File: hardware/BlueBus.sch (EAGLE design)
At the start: 128 parts, among them Q1 NMOSFET-BSS138K, Q2 PMOSFET-DMP1045UQ, Q3 NMOSFET-BSS138K, X1 CRYSTAL-12MHZ

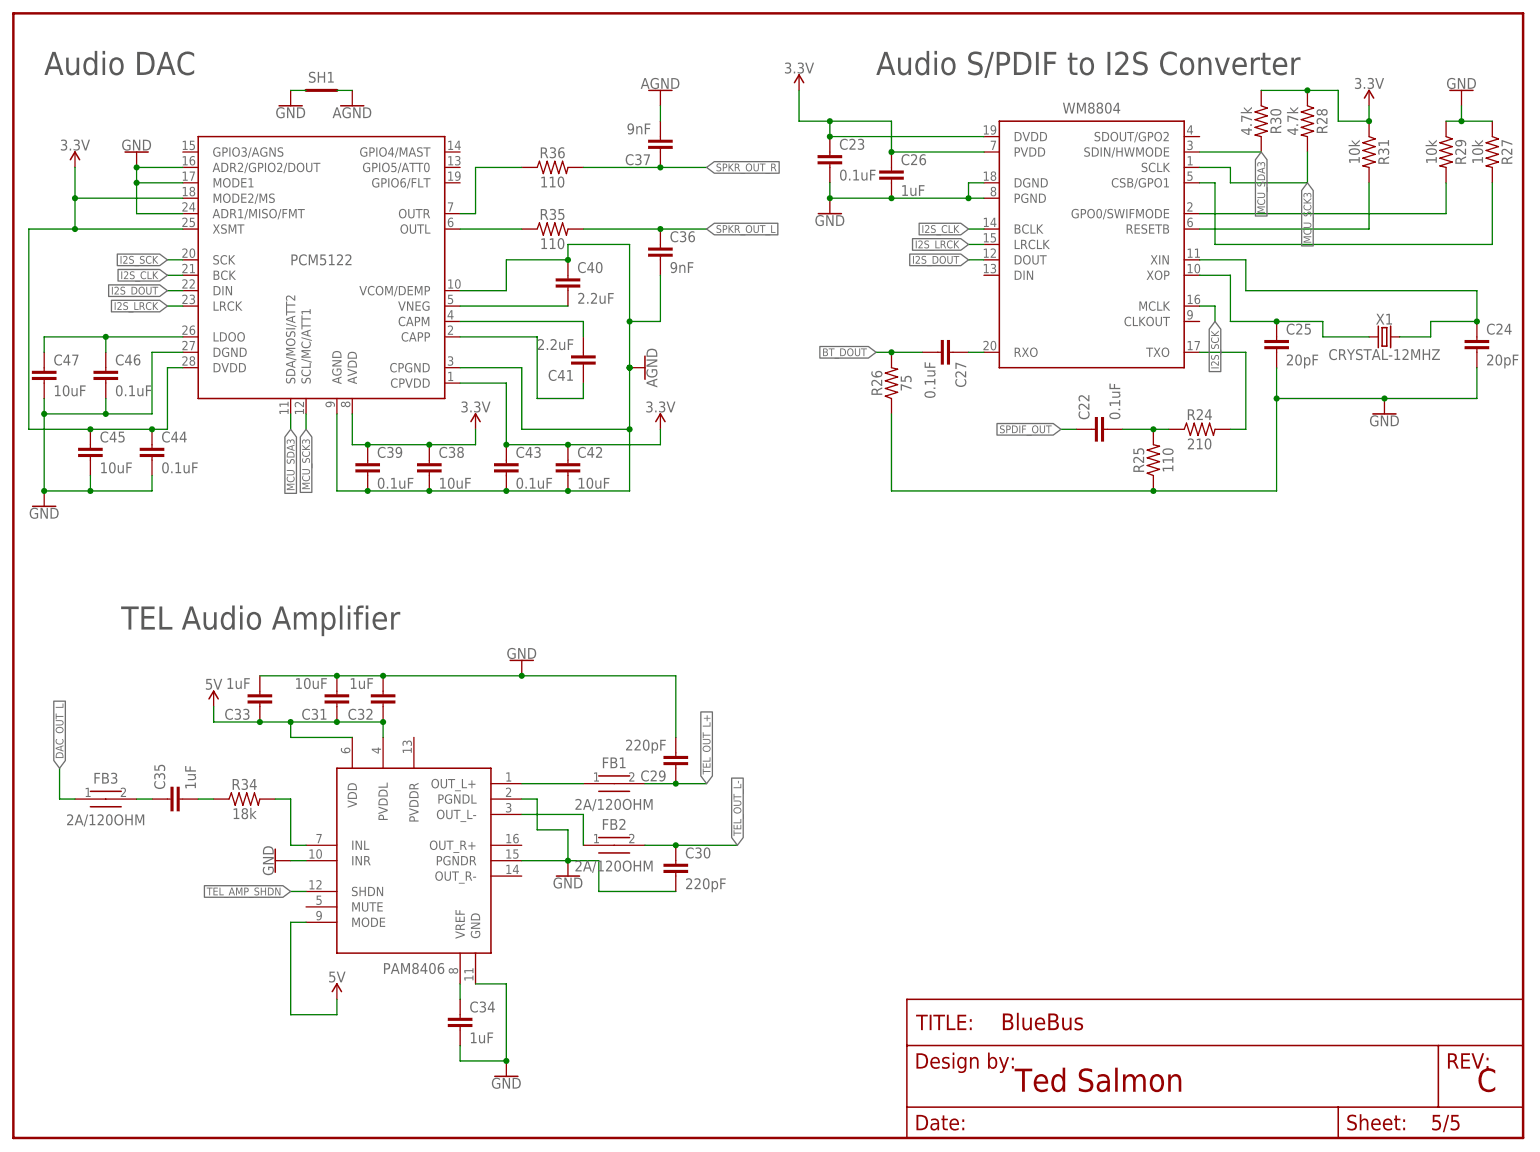
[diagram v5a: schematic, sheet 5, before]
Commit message: [IMP] hardware: V 1.2 * Power PAM8406 PVDDR and add bypass caps * Rework layout for PAM8406 and its passives * Connect floating VIAs to ground
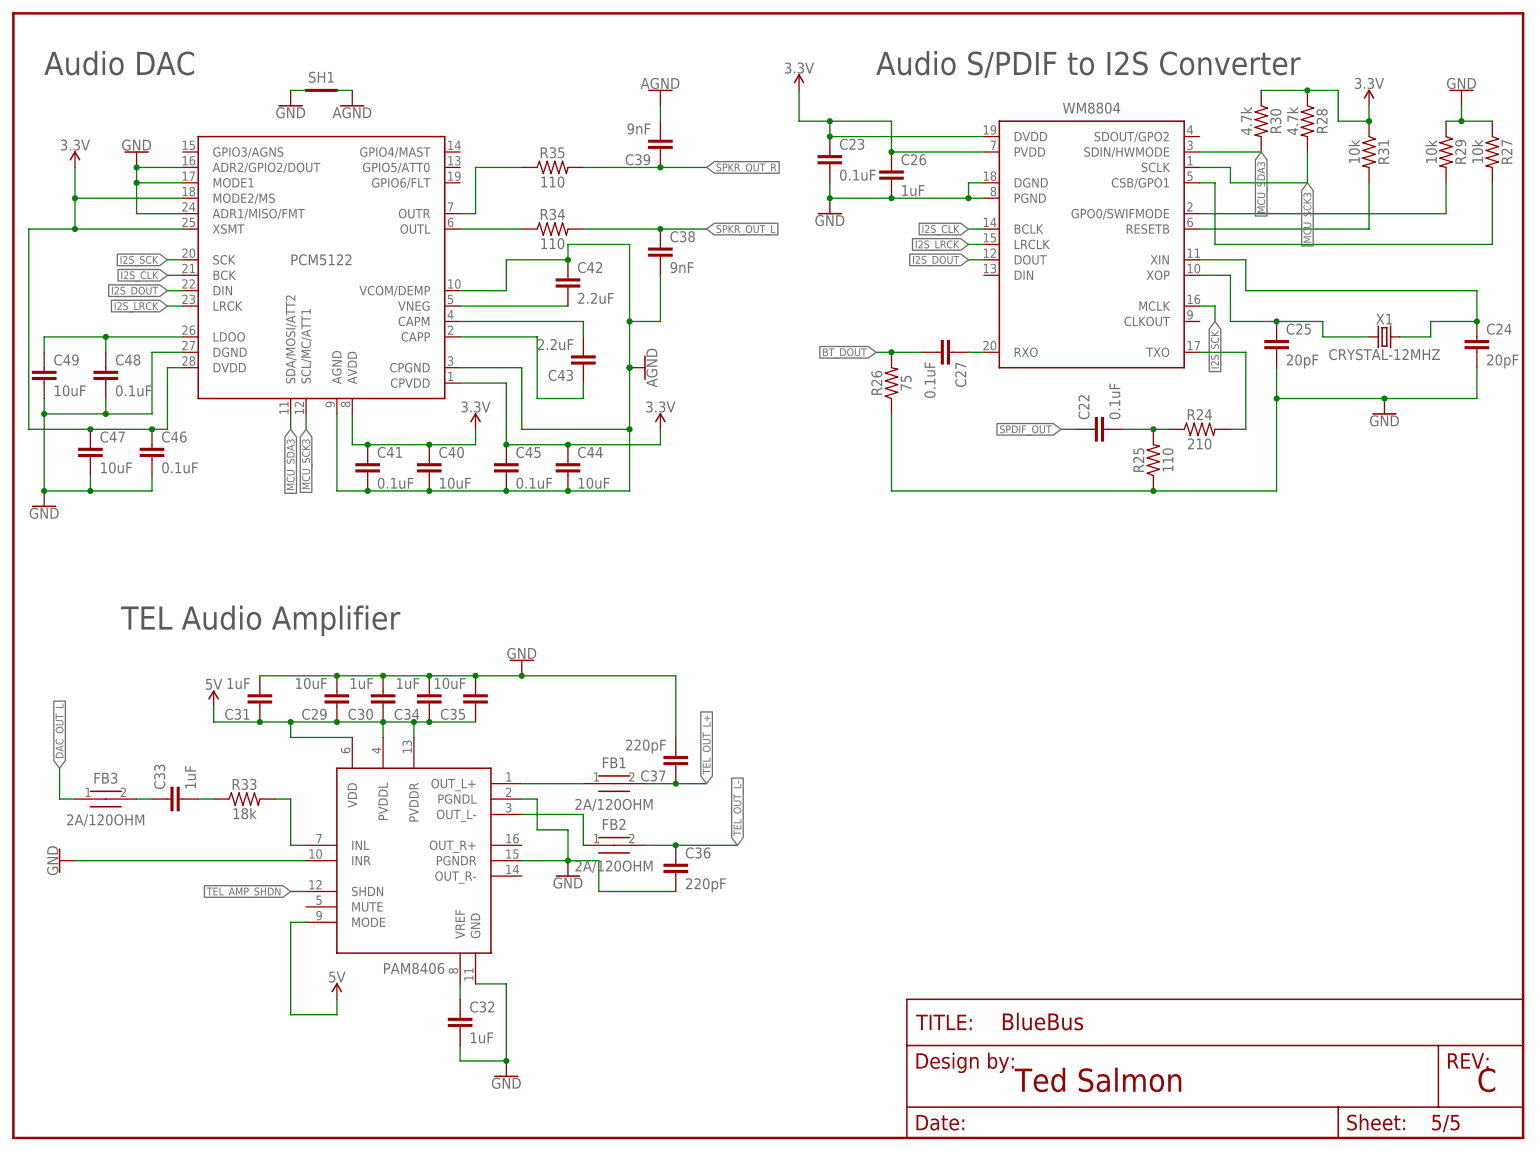
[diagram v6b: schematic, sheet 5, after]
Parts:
- removed R36: 110, Passives:110OHM
- added C48: 0.1uF, Passives:0.1UF
- added C49: 10uF, Passives:10UF2012
- added R33: 18k, Passives:18KOHM
- C29: value 220pF -> 10uF; device Passives:220PF -> Passives:10UF2012
- C30: value 220pF -> 1uF; device Passives:220PF -> Passives:1UF
- C31: value 10uF -> 1uF; device Passives:10UF2012 -> Passives:1UF
- C35: value 1uF -> 10uF; device Passives:1UF -> Passives:10UF2012
- C36, C37: value 9nF -> 220pF; device Passives:9NF -> Passives:220PF
- C38: value 10uF -> 9nF; device Passives:10UF2012 -> Passives:9NF
- C39: value 0.1uF -> 9nF; device Passives:0.1UF -> Passives:9NF
- C40: value 2.2uF -> 10uF; device Passives:2.2UF -> Passives:10UF2012
- C41: value 2.2uF -> 0.1uF; device Passives:2.2UF -> Passives:0.1UF
- C42: value 10uF -> 2.2uF; device Passives:10UF2012 -> Passives:2.2UF
- C43: value 0.1uF -> 2.2uF; device Passives:0.1UF -> Passives:2.2UF
- C44: value 0.1uF -> 10uF; device Passives:0.1UF -> Passives:10UF2012
- C45: value 10uF -> 0.1uF; device Passives:10UF2012 -> Passives:0.1UF
- Q2: value PMOSFET-DMP1045UQ -> PMOSFET-DMP32D4S; device Passives:PMOSFET-DMP1045UQ -> Passives:PMOSFET-DMP32D4S
- R32: value 2k -> 4.7k; device Passives:2KOHM -> Passives:4.7KOHM
- R34: value 18k -> 110; device Passives:18KOHM -> Passives:110OHM
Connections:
- net 3.3V: now also C40.1, C41.1, C46.1, C47.1; no longer C38.1, C39.1, C42.1, C43.1
- net 5V: now also C29.1, C30.1, C34.1, C35.1, PAM8406.PVDDR; no longer C32.1, C33.1
- net AGND: now also C40.2, C41.2, C42.1, C44.2, C45.2; no longer C36.2, C37.2, C40.1, C42.2, C43.2
- net DAC_CAPM: now also C43.2; no longer C41.2
- net DAC_CAPP: now also C43.1; no longer C41.1
- net DAC_LDOO: now also C48.1, C49.1; no longer C46.1, C47.1
- net DAC_OUT_L: now also R34.1; no longer R35.1
- net DAC_OUT_R: now also R35.1; no longer R36.1
- net DAC_VNEG: now also C42.2; no longer C40.2
- net GND: now also C35.2, C36.2, C37.2, C48.2, C49.2; no longer C33.2, C44.2, C45.2
- net SPKR_OUT_L: now also C38.1, R34.2; no longer C36.1, R35.2
- net SPKR_OUT_R: now also C39.1, R35.2; no longer C37.1, R36.2
- net TEL_AMP_IN: now also C33.1; no longer C35.1
- net TEL_AMP_INL: now also R33.2; no longer R34.2
- net TEL_AMP_INL_CAP_RES: now also C33.2, R33.1; no longer C35.2, R34.1
- net TEL_AMP_VREF: now also C32.1; no longer C34.1
- net TEL_OUT_L+: now also C37.1; no longer C29.1
- net TEL_OUT_L-: now also C36.1; no longer C30.1
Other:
- moved on the sheet: C29, C30, C31, C32, C33, C34, C35, C36, C37, C38, C39, C40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
